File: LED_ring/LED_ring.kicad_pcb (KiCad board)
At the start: 2 copper layers, 15 parts, among them U1 BC546

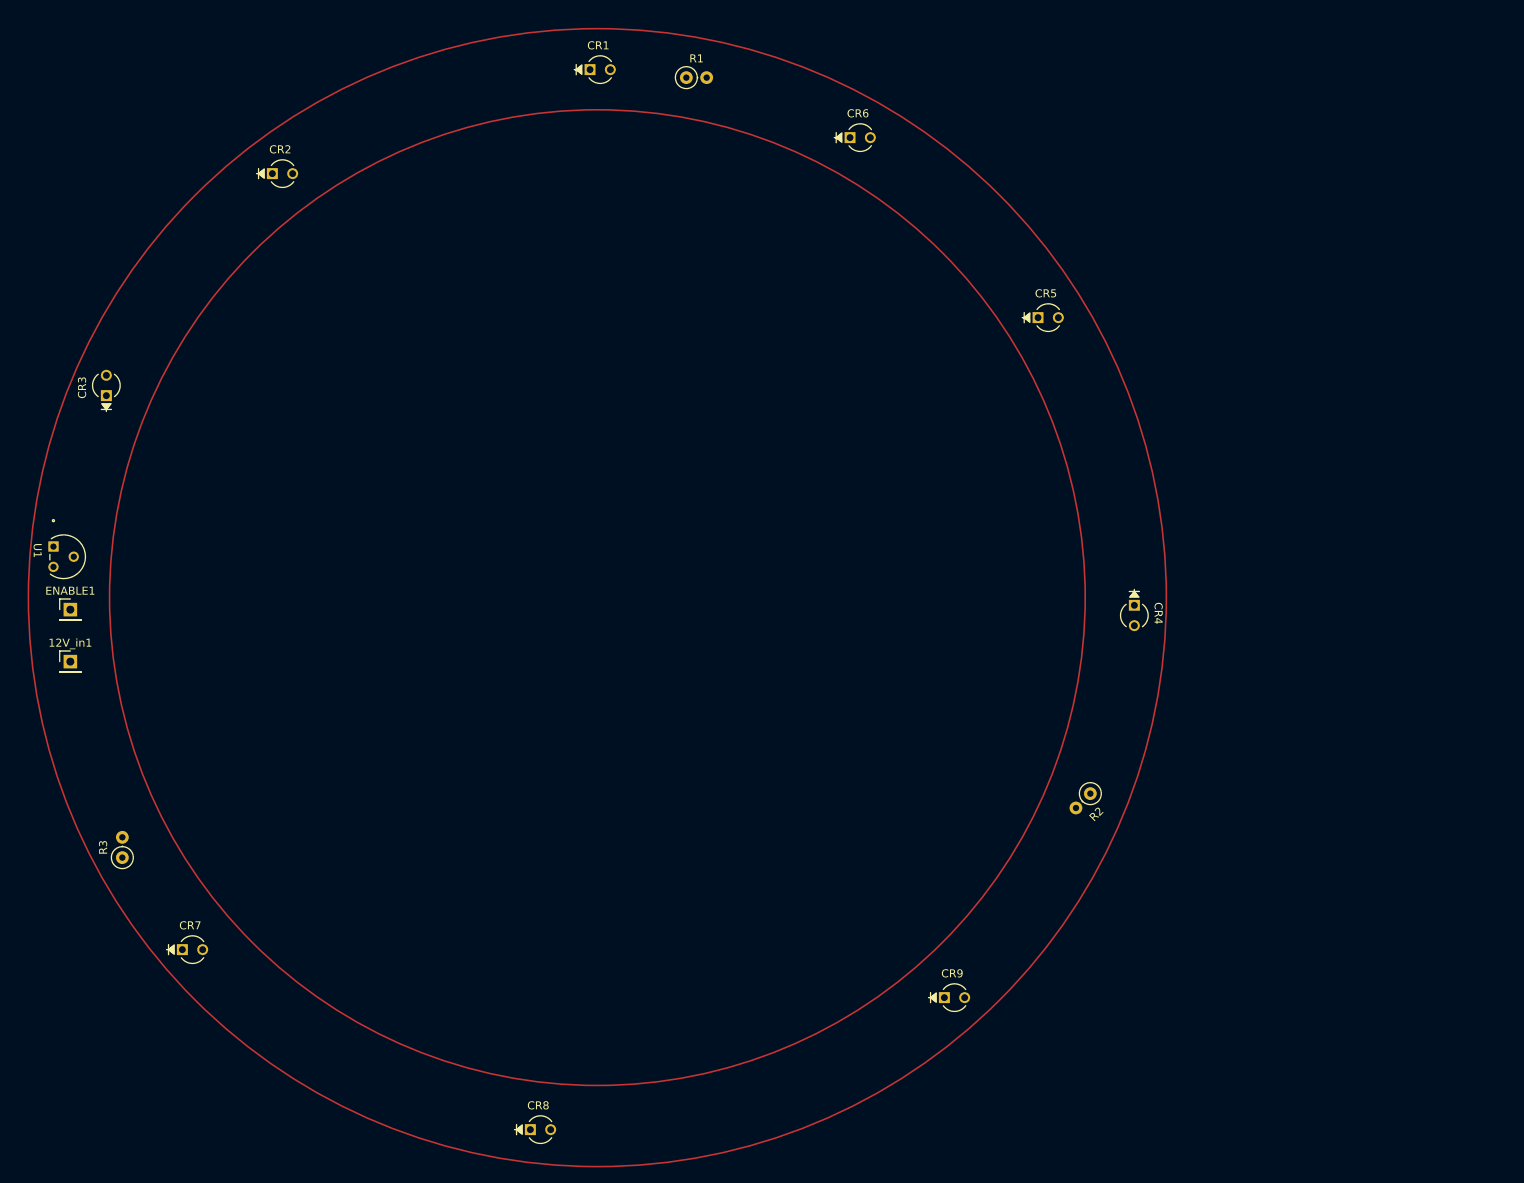
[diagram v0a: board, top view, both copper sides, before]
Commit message: Modified to fit with new spec
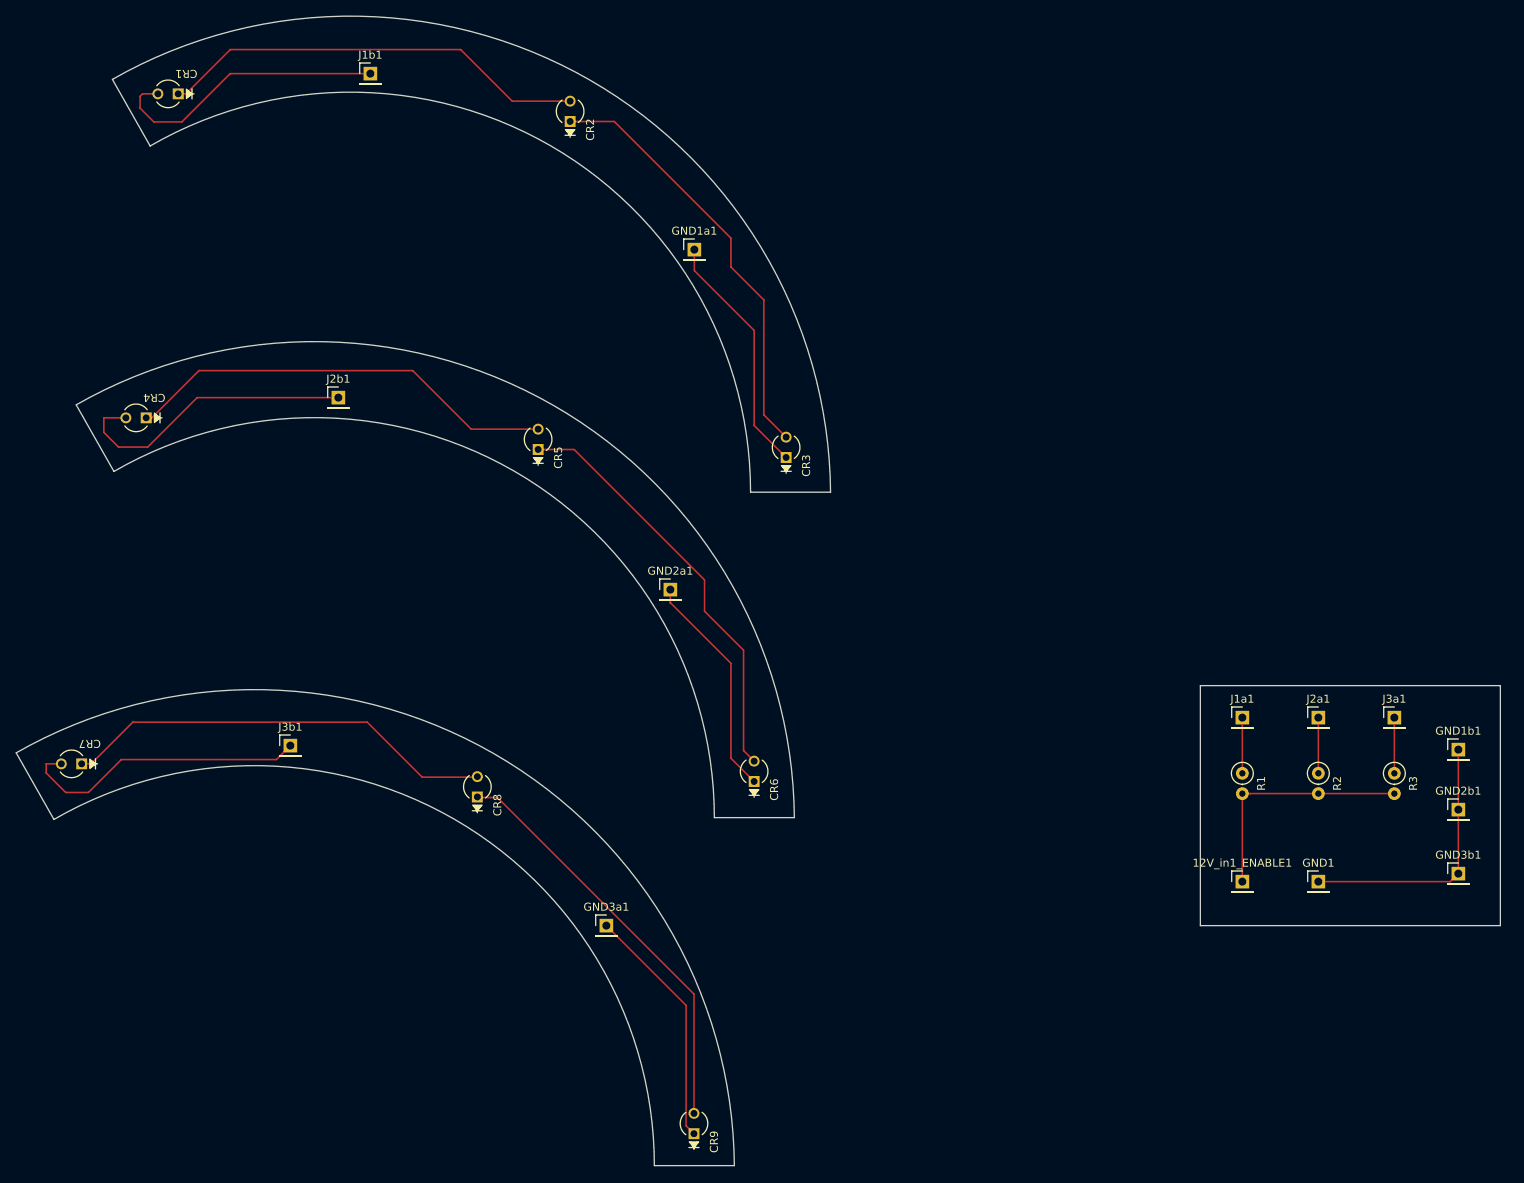
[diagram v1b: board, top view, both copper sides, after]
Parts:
- removed U1: BC546, Mechatronics:TO-92_ONS
- added GND1a1: Conn_01x01_Pin, Connector_PinHeader_2.54mm:PinHeader_1x01_P2.54mm_Vertical, F.Cu at (105.0, 50.0)
- added GND1b1: Conn_01x01_Pin, Connector_PinHeader_2.54mm:PinHeader_1x01_P2.54mm_Vertical, F.Cu at (200.5, 112.5)
- added GND2a1: Conn_01x01_Pin, Connector_PinHeader_2.54mm:PinHeader_1x01_P2.54mm_Vertical, F.Cu at (102.0, 92.5)
- added GND2b1: Conn_01x01_Pin, Connector_PinHeader_2.54mm:PinHeader_1x01_P2.54mm_Vertical, F.Cu at (200.5, 120.0)
- added GND3a1: Conn_01x01_Pin, Connector_PinHeader_2.54mm:PinHeader_1x01_P2.54mm_Vertical, F.Cu at (94.0, 134.5)
- added GND3b1: Conn_01x01_Pin, Connector_PinHeader_2.54mm:PinHeader_1x01_P2.54mm_Vertical, F.Cu at (200.5, 128.0)
- added J1a1: Conn_01x01_Pin, Connector_PinHeader_2.54mm:PinHeader_1x01_P2.54mm_Vertical, F.Cu at (173.5, 108.5)
- added J1b1: Conn_01x01_Pin, Connector_PinHeader_2.54mm:PinHeader_1x01_P2.54mm_Vertical, F.Cu at (64.5, 28.0)
- added J2a1: Conn_01x01_Pin, Connector_PinHeader_2.54mm:PinHeader_1x01_P2.54mm_Vertical, F.Cu at (183.0, 108.5)
- added J2b1: Conn_01x01_Pin, Connector_PinHeader_2.54mm:PinHeader_1x01_P2.54mm_Vertical, F.Cu at (60.5, 68.5)
- added J3a1: Conn_01x01_Pin, Connector_PinHeader_2.54mm:PinHeader_1x01_P2.54mm_Vertical, F.Cu at (192.5, 108.5)
- added J3b1: Conn_01x01_Pin, Connector_PinHeader_2.54mm:PinHeader_1x01_P2.54mm_Vertical, F.Cu at (54.5, 112.0)
- CR1, CR2, CR3, CR4, CR5, CR6, CR7, CR8, CR9: footprint Mechatronics:TLL_Series_VIS -> LED_ring:TLL_Series_VIS
- R1, R2, R3: value 180 -> 100
- moved GND1 159.7 mm to (183.0, 129.0)
- moved R3 159.3 mm to (192.5, 115.5), turned to -90 degrees
- moved 12V_in1_ENABLE1 149.1 mm to (173.5, 129.0)
- moved CR4 126.7 mm to (35.5, 71.0), turned to 180 degrees
- moved R1 111.3 mm to (173.5, 115.5), turned to -90 degrees
- moved CR3 85.3 mm to (116.5, 75.0)
- moved CR6 80.4 mm to (112.5, 115.5), turned to 90 degrees
- moved CR5 64.4 mm to (85.5, 74.0), turned to 90 degrees
- moved CR1 52.5 mm to (39.5, 30.5), turned to 180 degrees
- moved CR8 43.1 mm to (77.9, 117.4), turned to 90 degrees
- moved CR2 38.0 mm to (89.5, 33.0), turned to 90 degrees
- moved CR9 35.1 mm to (105.0, 159.5), turned to 90 degrees
- moved R2 28.6 mm to (183.0, 115.5), turned to -90 degrees
- moved CR7 26.9 mm to (27.4, 114.2), turned to 180 degrees
- renumbered 12V_in1 to 12V_in1_ENABLE1, ENABLE1 to GND1
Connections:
- CR1 pad 2: Net-(CR1-Pad2) -> Net-(J1b1-Pin_1)
- CR3 pad 1: Net-(U1-C) -> Net-(GND1a1-Pin_1)
- CR4 pad 2: Net-(CR4-Pad2) -> Net-(J2b1-Pin_1)
- CR6 pad 1: Net-(U1-C) -> Net-(GND2a1-Pin_1)
- CR7 pad 2: Net-(CR7-Pad2) -> Net-(J3b1-Pin_1)
- CR9 pad 1: Net-(U1-C) -> Net-(GND3a1-Pin_1)
- R1 pad 1: Net-(CR1-Pad2) -> Net-(J1a1-Pin_1)
- R2 pad 1: Net-(CR4-Pad2) -> Net-(J2a1-Pin_1)
- R3 pad 1: Net-(CR7-Pad2) -> Net-(J3a1-Pin_1)
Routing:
- net Net-(CR7-Pad1): track 0.00 -> 55.1 mm
- net Net-(CR4-Pad1): track 0.00 -> 54.5 mm
- net Net-(CR1-Pad1): track 0.00 -> 54.0 mm
- net Net-(CR2-Pad1): track 0.00 -> 53.9 mm
- net Net-(CR5-Pad1): track 0.00 -> 52.8 mm
- net Net-(CR8-Pad1): track 0.00 -> 51.6 mm
- net Net-(J2b1-Pin_1): track 0.00 -> 37.2 mm
- net Net-(J3b1-Pin_1): track 0.00 -> 37.0 mm
- net Net-(J1b1-Pin_1): track 0.00 -> 35.8 mm
- net Net-(GND1-Pin_1): track 0.00 -> 33.4 mm
- net Net-(GND1a1-Pin_1): track 0.00 -> 30.7 mm
- net Net-(GND3a1-Pin_1): track 0.00 -> 30.5 mm
- net Net-(12V_in1_ENABLE1-Pin_1): track 0.00 -> 30.0 mm
- net Net-(GND2a1-Pin_1): track 0.00 -> 28.4 mm
- net Net-(J3a1-Pin_1): track 0.00 -> 6.96 mm
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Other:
- board outline added: 185.5 x 143.7 mm

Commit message: Finalized PCB design
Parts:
- R1, R2, R3: footprint Resistor_THT:R_Axial_DIN0207_L6.3mm_D2.5mm_P2.54mm_Vertical -> Resistor_THT:R_Axial_DIN0204_L3.6mm_D1.6mm_P5.08mm_Horizontal
- moved GND3b1 1.26 mm to (200.6, 129.3)
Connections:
- CR9 pad 1: Net-(GND3a1-Pin_1) -> Net-(CR8-Pad1)
- GND3a1 pad 1: Net-(GND3a1-Pin_1) -> Net-(CR8-Pad1)
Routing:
- net Net-(CR8-Pad1): track 51.6 -> 83.5 mm
- net Net-(GND3a1-Pin_1): track 30.5 -> 0.00 mm
- net Net-(12V_in1_ENABLE1-Pin_1): track 30.0 -> 27.5 mm
- net Net-(J2b1-Pin_1): track 37.2 -> 35.3 mm
- net Net-(GND1-Pin_1): track 33.4 -> 34.7 mm
- net Net-(GND1a1-Pin_1): track 30.7 -> 31.6 mm
- net Net-(CR2-Pad1): track 53.9 -> 54.6 mm
- net Net-(CR7-Pad1): track 55.1 -> 54.5 mm

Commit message: Finalized PCB design
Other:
- board size 185.5 x 143.7 mm -> 186.4 x 143.7 mm
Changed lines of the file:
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@@
 	(gr_arc
 		(start 24.948186 121.228668)
-		(mid 74.97408 121.183757)
+		(mid 74.974083 121.183759)
 		(end 100 164.499982)
 		(stroke
@@
 	(gr_arc
 		(start 32.448186 77.728668)
-		(mid 82.47408 77.683757)
+		(mid 82.474083 77.683759)
 		(end 107.5 120.999982)
 		(stroke
@@
 	(gr_arc
 		(start 20.23063 112.903586)
-		(mid 79.900164 112.978543)
+		(mid 79.900167 112.978545)
 		(end 110 164.499983)
 		(stroke
@@
 	(gr_arc
 		(start 32.25655 28.719829)
-		(mid 91.926084 28.794786)
+		(mid 91.926085 28.794787)
 		(end 122.02592 80.316226)
 		(stroke
@@
 	(gr_arc
 		(start 27.73063 69.403586)
-		(mid 87.400164 69.478543)
+		(mid 87.400167 69.478545)
 		(end 117.5 120.999983)
 		(stroke
@@
 	(gr_arc
 		(start 36.974106 37.044911)
-		(mid 87 37)
+		(mid 86.999998 36.999999)
 		(end 112.02592 80.316225)
 		(stroke
@@
 	)
 	(gr_rect
-		(start 168.25 104.5)
-		(end 205.75 134.5)
+		(start 167.4622 103.378)
+		(end 206.629 135.2042)
 		(stroke
 			(width 0.05)
